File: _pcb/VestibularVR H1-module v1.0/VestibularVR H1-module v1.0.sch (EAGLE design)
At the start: 70 parts, among them IC1 FT232RL, IC2 74LVC1G07DBV, IC3 TLV70033DDCR, IC4 74LVC1G07DBV, IC5 74LVC1G07DBV, IC6 74LVC1G07DBV, IC7 USBLC6-2SC6, IC8 ATXMEGA32A4U, X1 TSW-105-02-S-D, X2 TSW-105-02-S-D, X7 22-23-2051

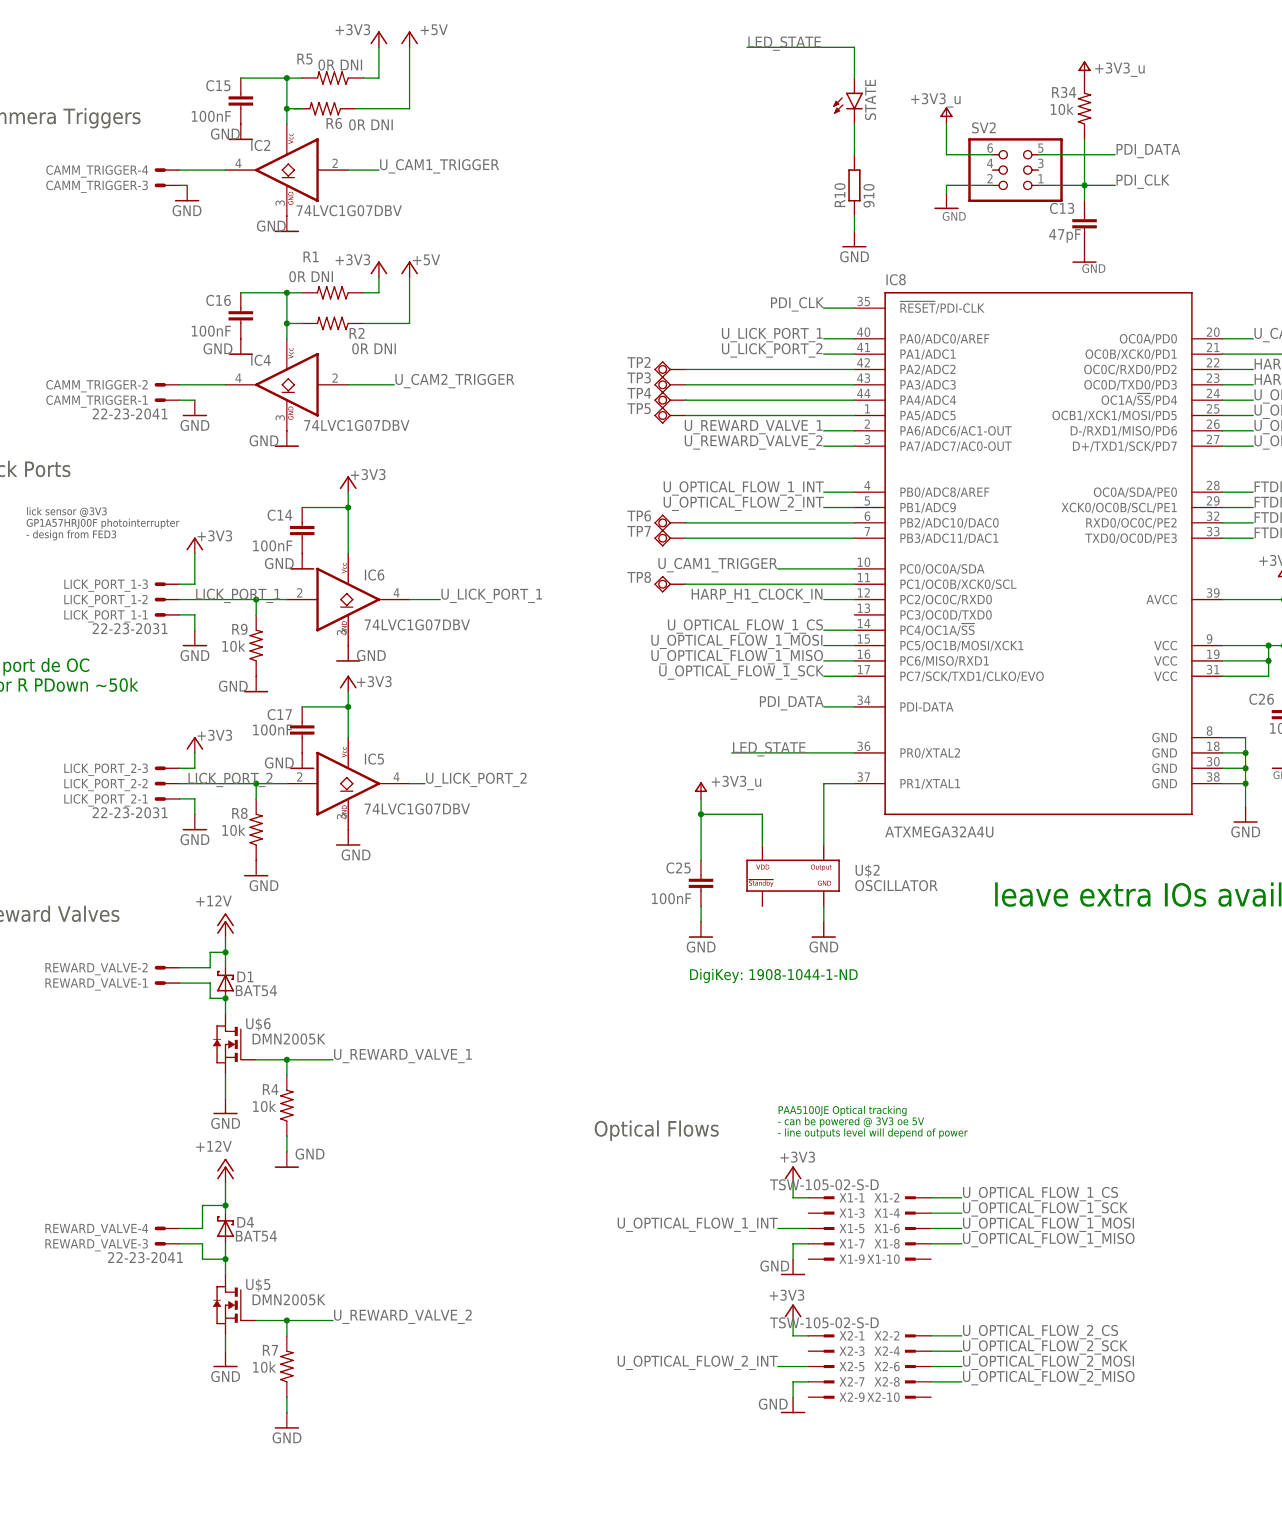
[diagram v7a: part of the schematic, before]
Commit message: . 1st stage pcb design finnalized . missing:   . put couple test poitns   . move mechanical hole from one to other side usb plug . Filipe going to do a revision
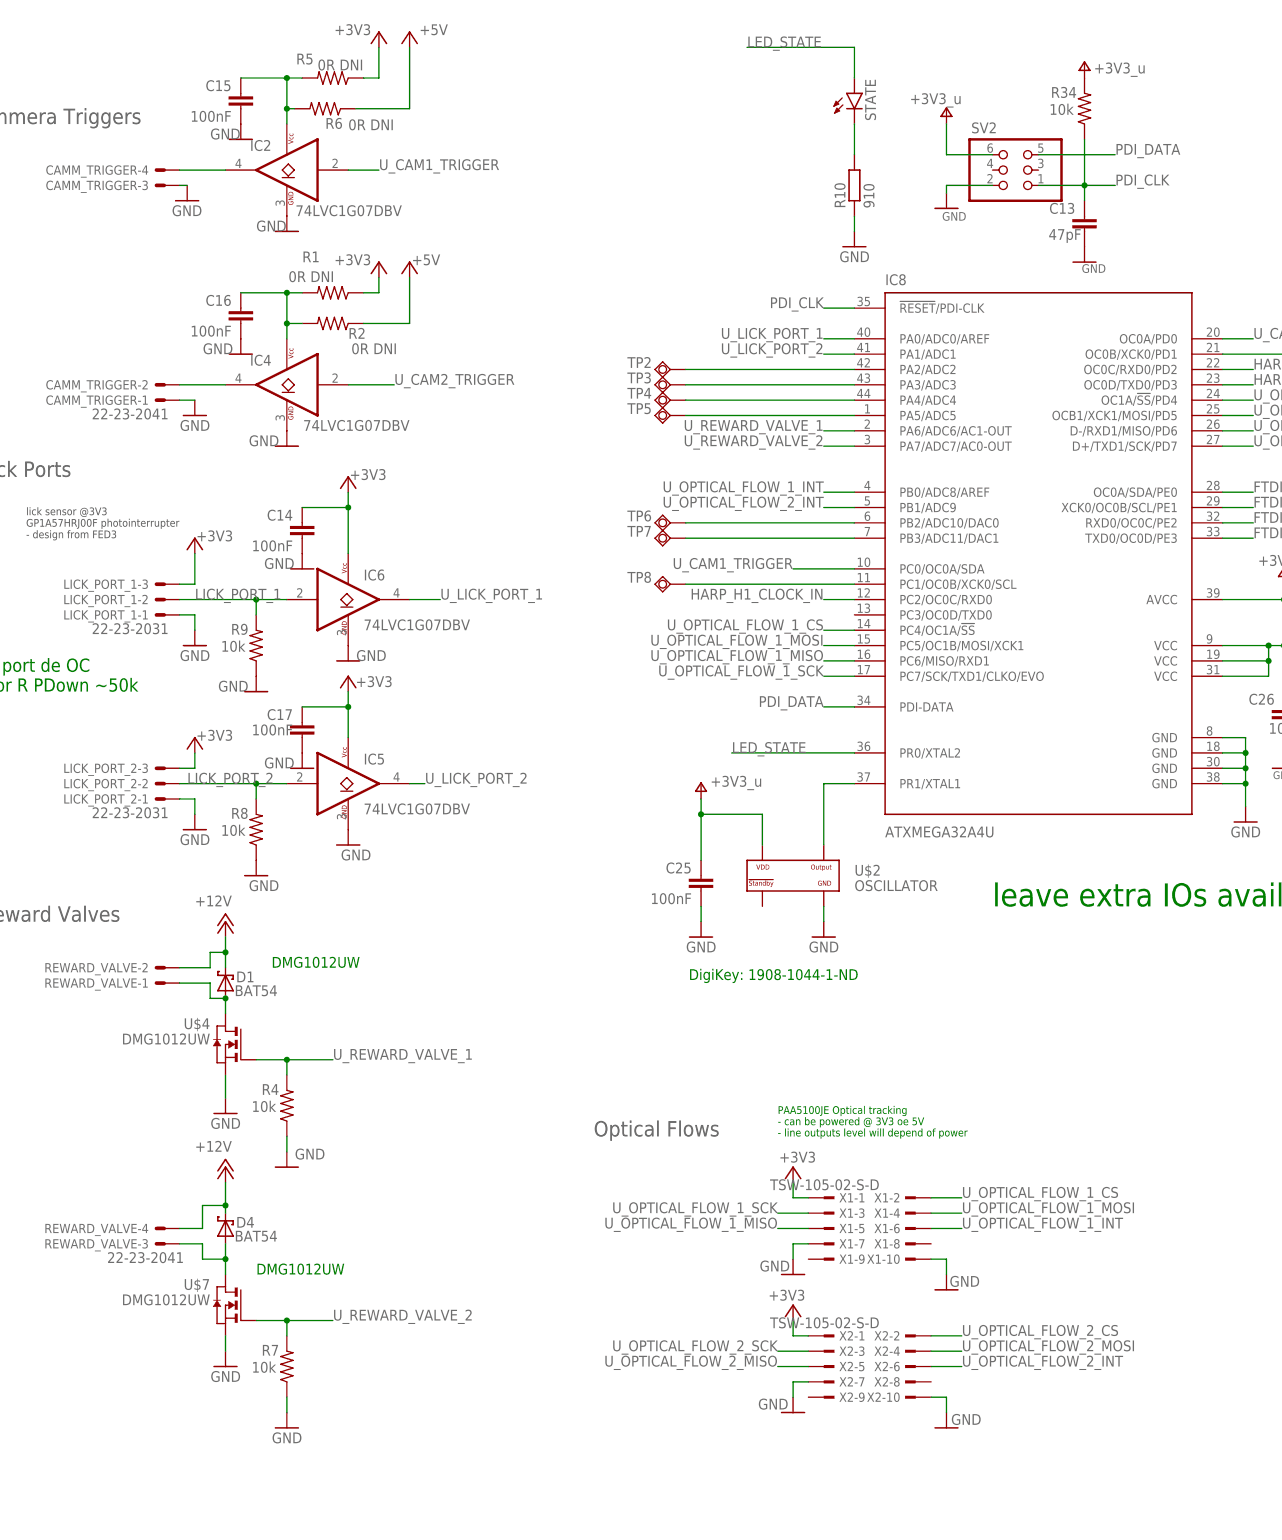
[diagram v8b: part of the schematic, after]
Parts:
- removed U$5, U$6: DMN2005K, VestibularVR H1-module v1.0:DMN2005K
- added U$4, U$7: DMG1012UW, VestibularVR H1-module v1.0:DMG1012UW-7
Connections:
- removed net N$7: D1.A, REWARD_VALVE-1.S, U$6.D
- new net N$68: D1.A, REWARD_VALVE-1.S, U$4.D
- net GND: now also U$4.S, U$7.S, X1-10.1, X2-10.1; no longer U$5.S, U$6.S
- net N$6: now also U$7.D; no longer U$5.D
- net U_OPTICAL_FLOW_1_INT: now also X1-6.1; no longer X1-5.1
- net U_OPTICAL_FLOW_1_MISO: now also X1-5.1; no longer X1-8.1
- net U_OPTICAL_FLOW_1_MOSI: now also X1-4.1; no longer X1-6.1
- net U_OPTICAL_FLOW_1_SCK: now also X1-3.1; no longer X1-4.1
- net U_OPTICAL_FLOW_2_INT: now also X2-6.1; no longer X2-5.1
- net U_OPTICAL_FLOW_2_MISO: now also X2-5.1; no longer X2-8.1
- net U_OPTICAL_FLOW_2_MOSI: now also X2-4.1; no longer X2-6.1
- net U_OPTICAL_FLOW_2_SCK: now also X2-3.1; no longer X2-4.1
- net U_REWARD_VALVE_1: now also U$4.G; no longer U$6.G
- net U_REWARD_VALVE_2: now also U$7.G; no longer U$5.G
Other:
- note added: "DMG1012UW"
